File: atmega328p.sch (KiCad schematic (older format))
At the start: 36 parts, among them CON1 Micro USB, CON2 AVR-ISP-6, IC1 DS3231M, IC2 LD1117, IC3 ATMEGA328-P, M1 D1, SW1 RESET, X1 16 MHz

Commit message: change batt holder due to wrong footprint
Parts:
- BATT1: footprint open-project:BAT_CR1216 -> .pretty:20mmBattHolder
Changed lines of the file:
@@
 F 0 "BATT1" H 4350 7000 50  0000 L CNN
 F 1 "CR2032" H 4350 6900 50  0000 L CNN
-F 2 "open-project:BAT_CR1216" V 4250 6990 50  0001 C CNN
+F 2 ".pretty:20mmBattHolder" V 4250 6990 50  0001 C CNN
 F 3 "" V 4250 6990 50  0000 C CNN
 	1    4250 6950

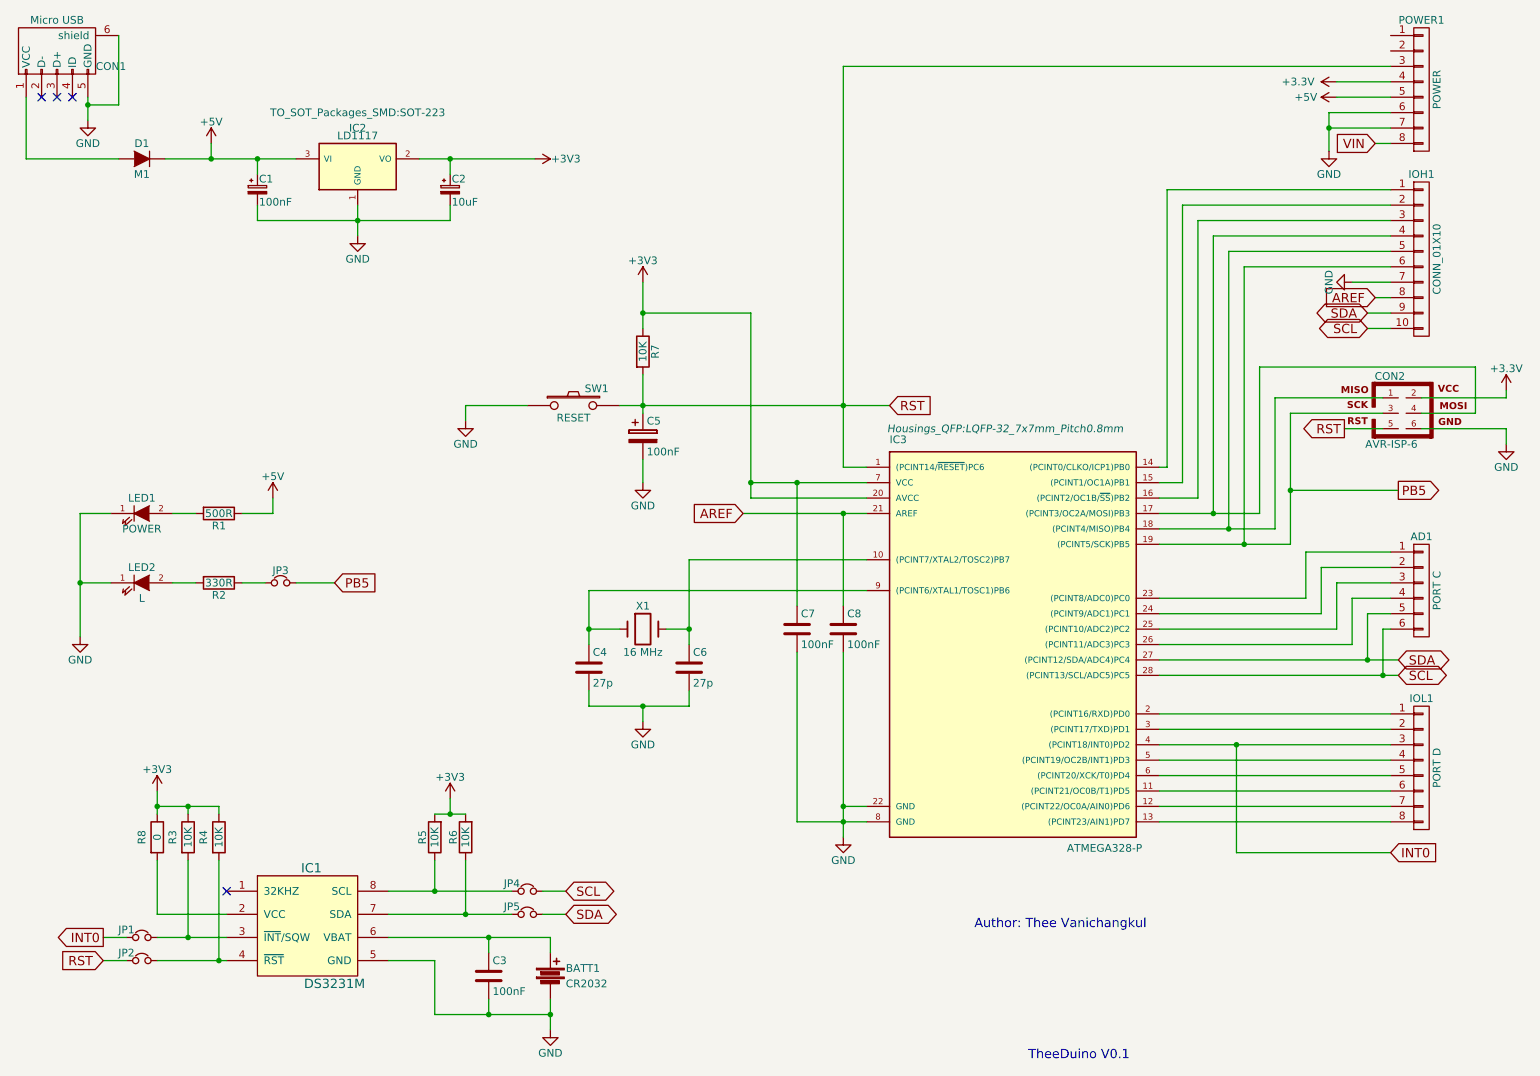
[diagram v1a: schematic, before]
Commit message: correct wrong footprint and pinout of atmega328p
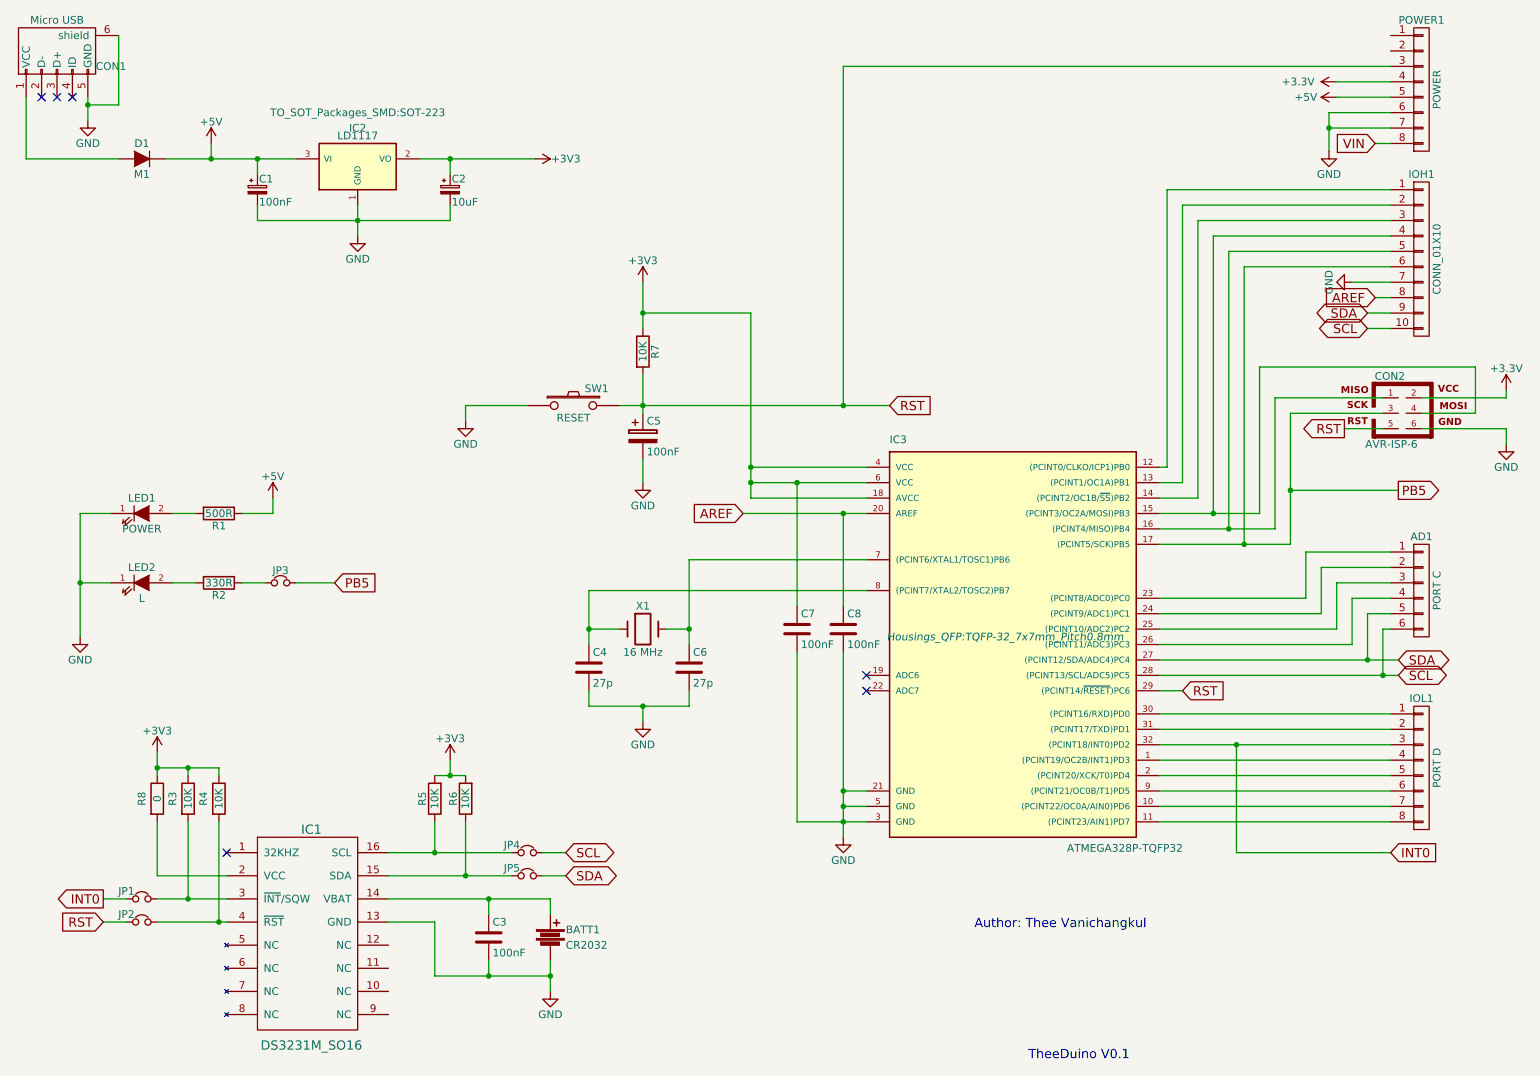
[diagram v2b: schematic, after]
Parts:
- removed IC1: DS3231M, Housings_SOIC:SOIC-8_3.9x4.9mm_Pitch1.27mm, symbol DS3231M-RESCUE-atmega328p
- removed IC3: ATMEGA328-P, Housings_QFP:LQFP-32_7x7mm_Pitch0.8mm, symbol ATMEGA328-P-RESCUE-atmega328p
- added IC1: DS3231M_SO16, Housings_SOIC:SOIC-16W_7.5x10.3mm_Pitch1.27mm, symbol DS3231M_SO16
- added IC3: ATMEGA328P-TQFP32, Housings_QFP:TQFP-32_7x7mm_Pitch0.8mm, symbol ATMEGA328P-TQFP32
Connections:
- net +3V3: now also IC3.18 (AVCC), IC3.4 (VCC), IC3.6 (VCC)
- net AREF: now also IC3.20 (AREF)
- net GND: now also IC1.13 (GND), IC3.21 (GND), IC3.3 (GND), IC3.5 (GND)
- net INT0: now also IC3.32 ((PCINT18/INT0)PD2)
- net PB5: now also IC3.17 ((PCINT5/SCK)PB5)
- net RST: now also IC3.29 ((PCINT14/~RESET~)PC6)
- net SCL: now also IC3.28 ((PCINT13/SCL/ADC5)PC5)
- net SDA: now also IC3.27 ((PCINT12/SDA/ADC4)PC4)
- net at C4.1, X1.1: now also IC3.8 ((PCINT7/XTAL2/TOSC2)PB7)
- net at C6.1, X1.2: now also IC3.7 ((PCINT6/XTAL1/TOSC1)PB6)
- net at CON2.1, IOH1.5 (P5): now also IC3.16 ((PCINT4/MISO)PB4)
- net at CON2.4, IOH1.4 (P4): now also IC3.15 ((PCINT3/OC2A/MOSI)PB3)
- net at IOL1.6 (P6): now also IC3.9 ((PCINT21/OC0B/T1)PD5)
- net at IOL1.7 (P7): now also IC3.10 ((PCINT22/OC0A/AIN0)PD6)
- net at IOL1.8 (P8): now also IC3.11 ((PCINT23/AIN1)PD7)
- net at IOH1.1 (P1): now also IC3.12 ((PCINT0/CLKO/ICP1)PB0)
- net at IOH1.2 (P2): now also IC3.13 ((PCINT1/OC1A)PB1)
- net at IOH1.3 (P3): now also IC3.14 ((PCINT2/OC1B/~SS~)PB2)
- net at IOL1.1 (P1): now also IC3.30 ((PCINT16/RXD)PD0)
- net at AD1.1 (P1): now also IC3.23 ((PCINT8/ADC0)PC0)
- net at AD1.2 (P2): now also IC3.24 ((PCINT9/ADC1)PC1)
- net at AD1.3 (P3): now also IC3.25 ((PCINT10/ADC2)PC2)
- net at AD1.4 (P4): now also IC3.26 ((PCINT11/ADC3)PC3)
- net at IOL1.2 (P2): now also IC3.31 ((PCINT17/TXD)PD1)
- net at IOL1.4 (P4): now also IC3.1 ((PCINT19/OC2B/INT1)PD3)
- net at IOL1.5 (P5): now also IC3.2 ((PCINT20/XCK/T0)PD4)
- net at R8.2: now also IC1.2 (VCC)
- net at JP1.2, R3.2: now also IC1.3 (~INT~/SQW)
- net at JP2.2, R4.2: now also IC1.4 (~RST~)
- net at BATT1.1, C3.1: now also IC1.14 (VBAT)
- net at JP5.1, R6.1: now also IC1.15 (SDA)
- net at JP4.1, R5.1: now also IC1.16 (SCL)
- no-connect marks 4 -> 6
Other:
- moved on the sheet: BATT1, C3, JP1, JP2, JP4, JP5, R3, R4, R5, R6, R8
